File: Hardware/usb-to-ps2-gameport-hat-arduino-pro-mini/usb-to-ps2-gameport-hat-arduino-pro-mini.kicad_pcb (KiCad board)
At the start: 2 copper layers, 50 x 40 mm, 27 parts, among them P1 Digital, P2 Analog

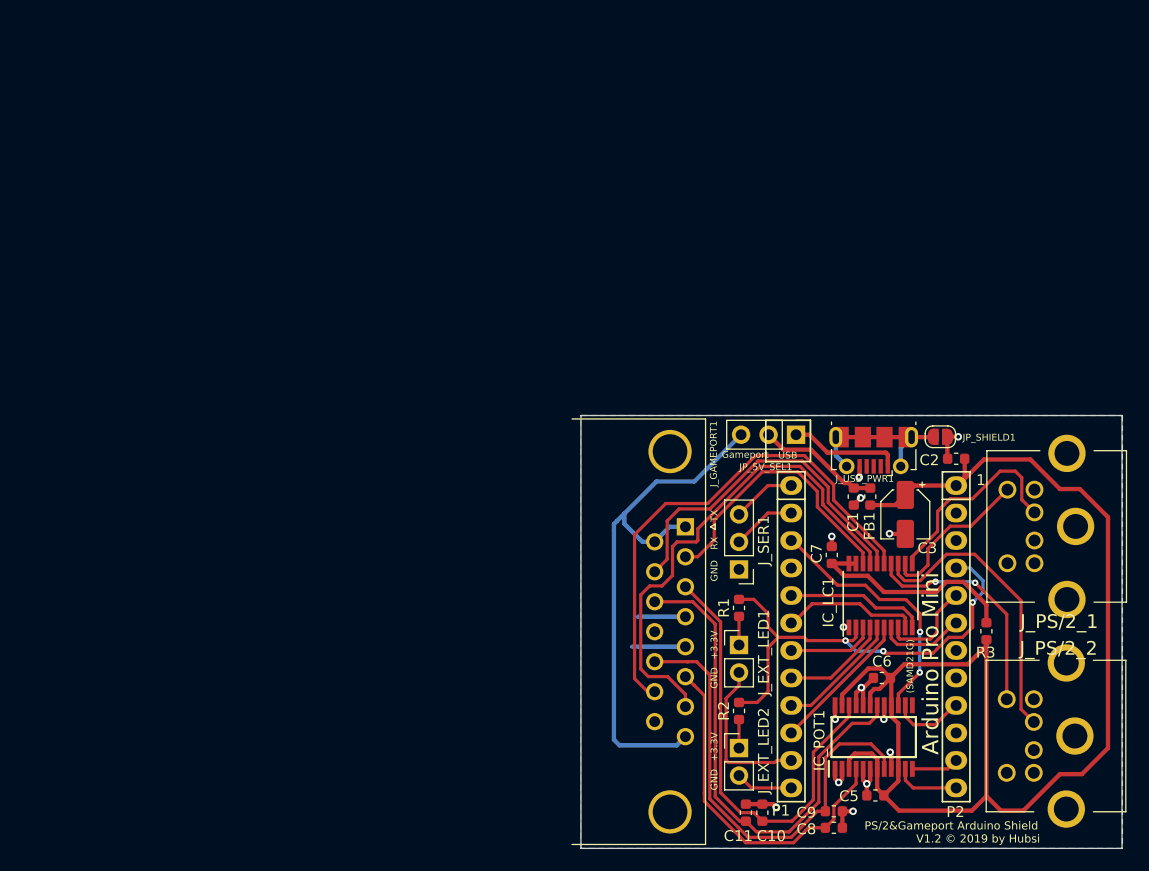
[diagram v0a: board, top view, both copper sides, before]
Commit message: update to KiCad 6
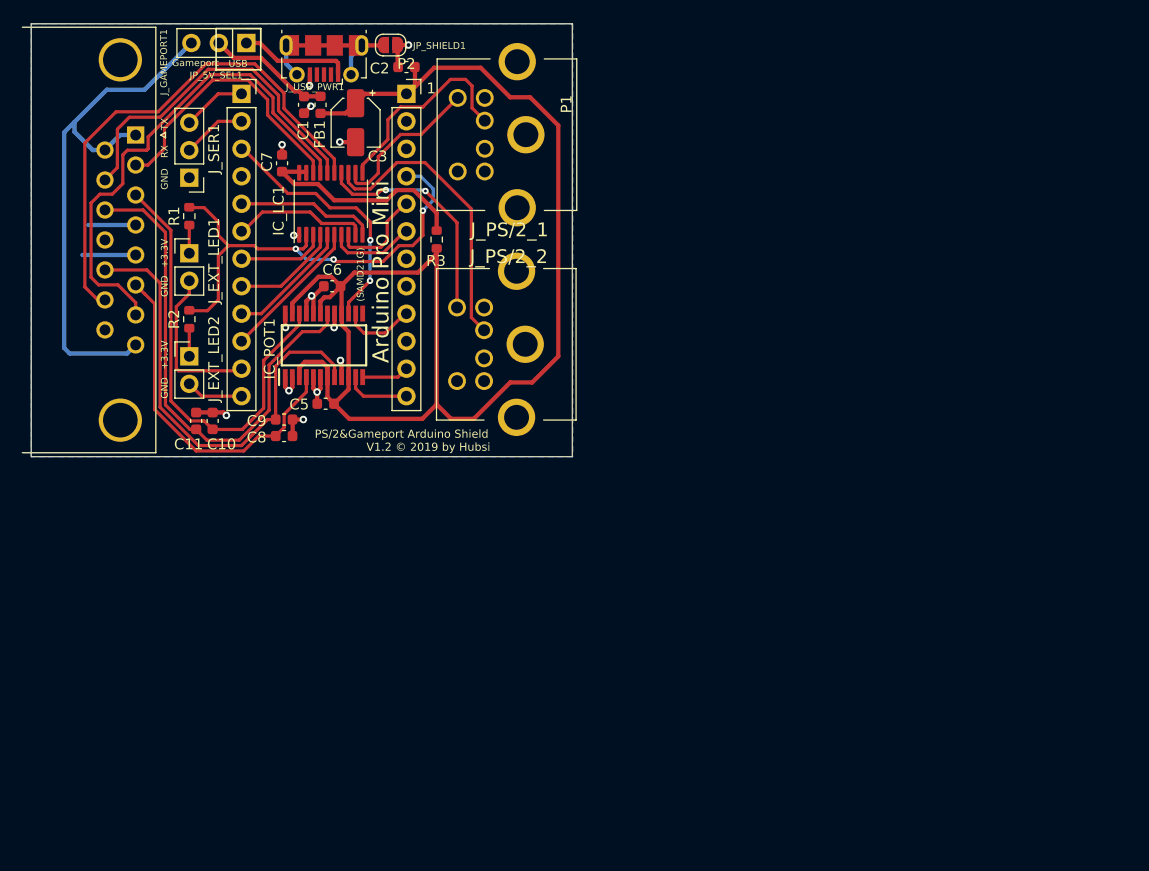
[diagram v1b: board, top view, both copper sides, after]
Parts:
- P1, P2: footprint Socket_Arduino_Pro_Mini:Socket_Strip_Arduino_1x12 -> Connector_PinSocket_2.54mm:PinSocket_1x12_P2.54mm_Vertical
- moved C6 62.4 mm to (114.2, 62.4)
- moved C10 62.4 mm to (103.1, 74.8)
- moved C11 62.4 mm to (101.6, 74.8)
- moved C3 62.4 mm to (116.3, 47.2)
- moved C7 62.4 mm to (109.5, 51.0)
- moved IC_POT1 62.4 mm to (113.4, 67.8)
- moved JP_5V_SEL1 62.4 mm to (106.2, 39.9)
- moved J_GAMEPORT1 62.4 mm to (96.0, 48.4)
- moved J_USB_PWR1 62.4 mm to (113.4, 41.3)
- moved P1 62.4 mm to (105.8, 44.6), turned to 0 degrees
- moved C8 62.4 mm to (109.7, 76.2)
- moved IC_LC1 62.4 mm to (114.0, 54.7)
- moved C2 62.4 mm to (121.0, 42.1)
- moved C5 62.4 mm to (113.6, 73.2)
- moved J_EXT_LED1 62.4 mm to (101.0, 59.3)
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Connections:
- IC_POT1 pad 13: (no net) -> unconnected-(IC_POT1-Pad13)
- J_GAMEPORT1 pad 12: (no net) -> unconnected-(J_GAMEPORT1-Pad12)
- J_GAMEPORT1 pad 15: (no net) -> unconnected-(J_GAMEPORT1-Pad15)
- J_PS/2_1 pad 2: (no net) -> unconnected-(J_PS/2_1-Pad2)
- J_PS/2_1 pad 4: (no net) -> unconnected-(J_PS/2_1-Pad4)
- J_PS/2_1 pad 6: (no net) -> unconnected-(J_PS/2_1-Pad6)
- J_PS/2_2 pad 2: (no net) -> unconnected-(J_PS/2_2-Pad2)
- J_PS/2_2 pad 4: (no net) -> unconnected-(J_PS/2_2-Pad4)
- J_PS/2_2 pad 6: (no net) -> unconnected-(J_PS/2_2-Pad6)
- J_USB_PWR1 pad 2: (no net) -> unconnected-(J_USB_PWR1-Pad2)
- J_USB_PWR1 pad 3: (no net) -> unconnected-(J_USB_PWR1-Pad3)
- J_USB_PWR1 pad 4: (no net) -> unconnected-(J_USB_PWR1-Pad4)
- P2 pad 10: (no net) -> /D12(MISO)
- P2 pad 3: (no net) -> unconnected-(P2-Pad3)
- P2 pad 7: (no net) -> unconnected-(P2-Pad7)
- P2 pad 8: (no net) -> unconnected-(P2-Pad8)
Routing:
- net +5V: track 130.0 -> 129.1 mm
- net /D5(JoyButton2): track 10.5 -> 9.83 mm
- net VCC: track 44.1 -> 43.6 mm
- net Net-(IC_LC1-Pad11): track 19.6 -> 19.1 mm
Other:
- net class Default removed
- net class Pwr removed

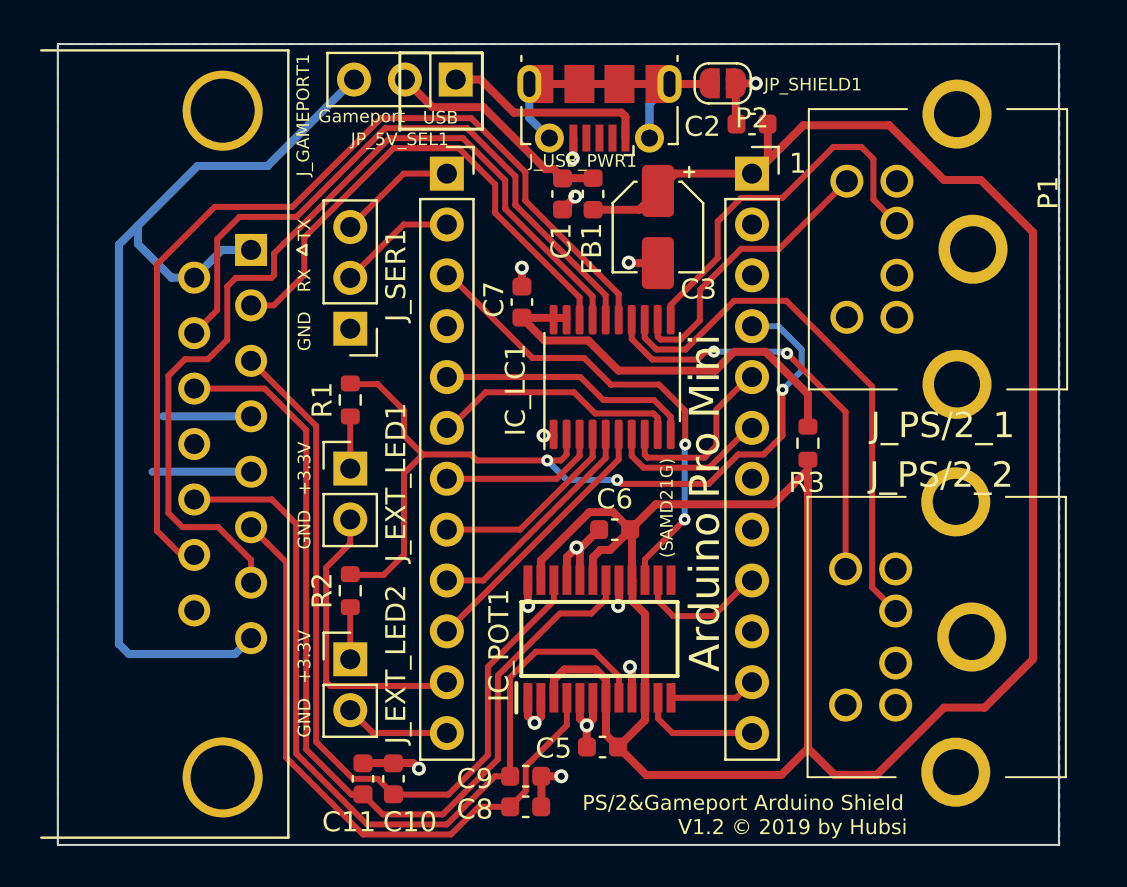
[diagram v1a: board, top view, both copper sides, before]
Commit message: Merge PR#1 from @Ulfenknulfen
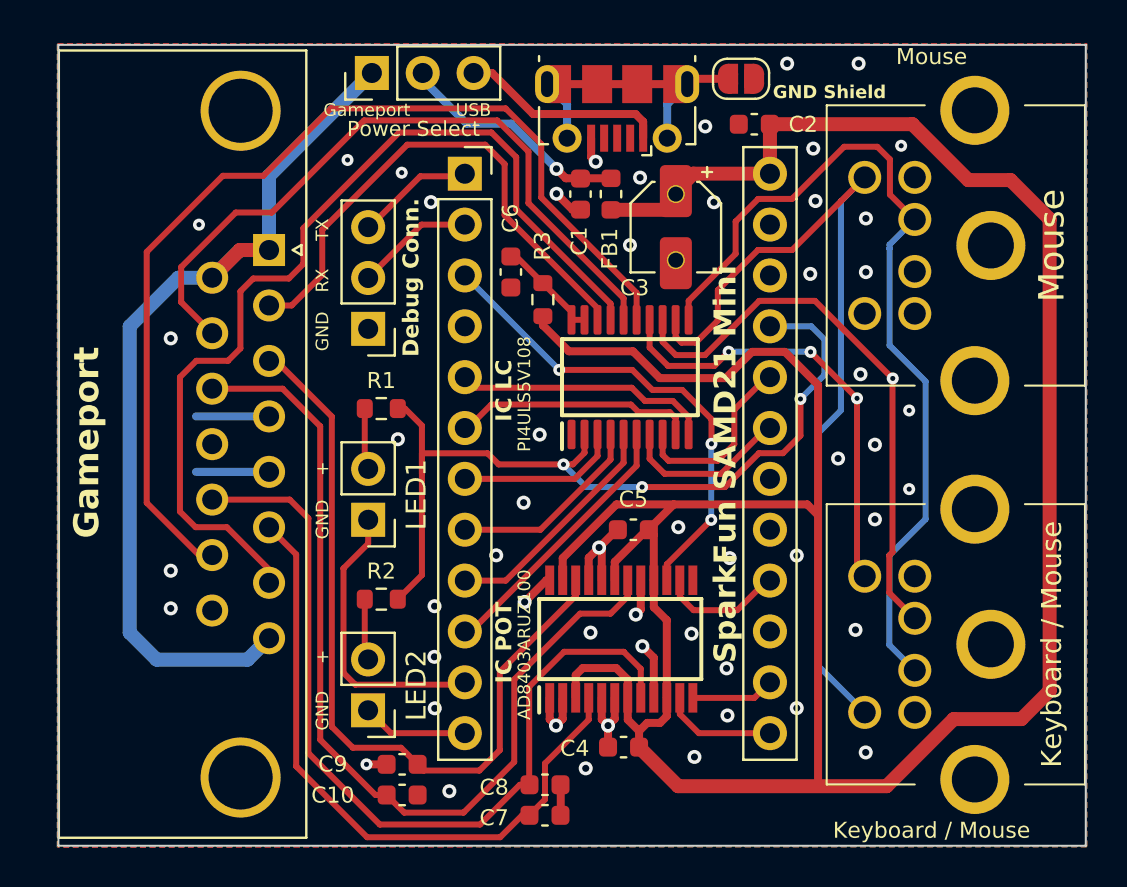
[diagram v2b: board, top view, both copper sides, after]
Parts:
- removed J_EXT_LED1, J_EXT_LED2: 2-pin header, Connector_PinHeader_2.54mm:PinHeader_1x02_P2.54mm_Vertical
- added ?: , , F.Cu at (117.2, 45.6)
- added ?: , , F.Cu at (117.2, 48.9)
- added LED1: 2-pin header, Connector_PinHeader_2.54mm:PinHeader_1x02_P2.54mm_Vertical, F.Cu at (101.9, 61.9)
- added LED2: 2-pin header, Connector_PinHeader_2.54mm:PinHeader_1x02_P2.54mm_Vertical, F.Cu at (101.9, 71.4)
- 5V Select1: renamed from JP_5V_SEL1
- Debug Conn1: renamed from J_SER1
- J_PS/2_1: value KMDGX-6S-BS -> Mouse
- J_PS/2_2: value KMDGX-6S-BS -> Keyboard / Mouse
- Shield GND1: renamed from JP_SHIELD1
- USB Power1: renamed from J_USB_PWR1
- moved R3 15.1 mm to (110.6, 50.9)
- moved 5V Select1 4.20 mm to (102.0, 39.5), turned to 90 degrees
- moved C10 2.12 mm to (103.6, 75.6), turned to 0 degrees
- moved R1 1.61 mm to (102.5, 56.3), turned to 180 degrees
- moved R2 1.61 mm to (102.5, 65.8), turned to 180 degrees
- moved C6 1.60 mm to (109.0, 49.5), turned to -90 degrees
- moved IC_POT1 1.09 mm to (114.5, 67.8)
- moved C4 1.05 mm to (114.6, 73.2)
- moved C7 1.05 mm to (110.7, 76.6)
- moved C8 1.05 mm to (110.7, 75.1)
- moved J_PS/2_2 1.02 mm to (129.2, 66.8)
- moved Shield GND1 0.94 mm to (120.5, 39.8)
- moved C5 0.93 mm to (115.1, 62.4)
- moved J_PS/2_1 0.91 mm to (129.2, 46.9)
- moved Gameport1 0.90 mm to (96.9, 48.4)
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- renumbered C11 to C10, C5 to C4, C6 to C5, C7 to C6, C8 to C7, C9 to C8, C10 to C9, J_GAMEPORT1 to Gameport1
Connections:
- 5V Select1 pad 1: /+5V(USB) -> /+5V(Gameport)
- 5V Select1 pad 2: Net-(C1-Pad1) -> unconnected-(5V Select1-C-Pad2)
- 5V Select1 pad 3: /+5V(Gameport) -> /+5V(USB)
- IC_LC1 pad 11: Net-(IC_LC1-Pad11) -> Net-(IC_LC1-B8)
- IC_LC1 pad 12: Net-(IC_LC1-Pad12) -> Net-(IC_LC1-B7)
- J_PS/2_1 pad 1: Net-(IC_LC1-Pad11) -> Net-(IC_LC1-B8)
- J_PS/2_1 pad 5: Net-(IC_LC1-Pad12) -> Net-(IC_LC1-B7)
- J_PS/2_2 pad 2: unconnected-(J_PS/2_2-Pad2) -> Net-(IC_LC1-B8)
- J_PS/2_2 pad 6: unconnected-(J_PS/2_2-Pad6) -> Net-(IC_LC1-B7)
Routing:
- net Net-(IC_LC1-B8): track 0.00 -> 43.9 mm
- net Net-(IC_LC1-B7): track 0.00 -> 43.5 mm
- net +5V: track 129.1 -> 149.0 mm
- net Net-(IC_LC1-Pad11): track 19.1 -> 0.00 mm
- net Net-(IC_LC1-EN): track 20.5 -> 5.23 mm
- net Net-(IC_LC1-Pad12): track 14.6 -> 0.00 mm
- net GND: track 38.7 -> 31.0 mm, vias 14 -> 54
- net /+5V(Gameport): track 50.1 -> 46.2 mm
- net Net-(Gameport1-P14): track 47.4 -> 51.0 mm
- net Net-(Gameport1-P10): track 32.3 -> 35.2 mm
- net Net-(IC_LC1-B2): track 46.6 -> 48.1 mm
- net /W1(Joy1X): track 41.0 -> 39.6 mm
- net Net-(IC_LC1-B6): track 27.1 -> 28.3 mm, vias 0 -> 1
- net Net-(IC_LC1-B5): track 21.4 -> 22.5 mm, vias 2 -> 3
- net /W2(Joy1Y): track 32.2 -> 33.2 mm
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- added copper zone on F.Cu, net GND
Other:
- board size 50 x 40 mm -> 51.3 x 40 mm
- board text added: "+"
- board text added: "Debug Conn."
- board text added: "GND Shield"
- board text added: "IC LC"
- board text added: "IC POT"
- board text added: "Keyboard / Mouse"
- board text added: "Mouse"
- board text added: "Power"
- board text added: "Power Select"
- board text added: "SparkFun SAMD21 Mini"
- board text added: "V1.3 © 2024 by Hubsi"
- board text removed: "(SAMD21G)"
- board text removed: "+3.3V"
- board text removed: "1"
- board text removed: "Arduino Pro Mini"
- board text removed: "V1.2 © 2019 by Hubsi"

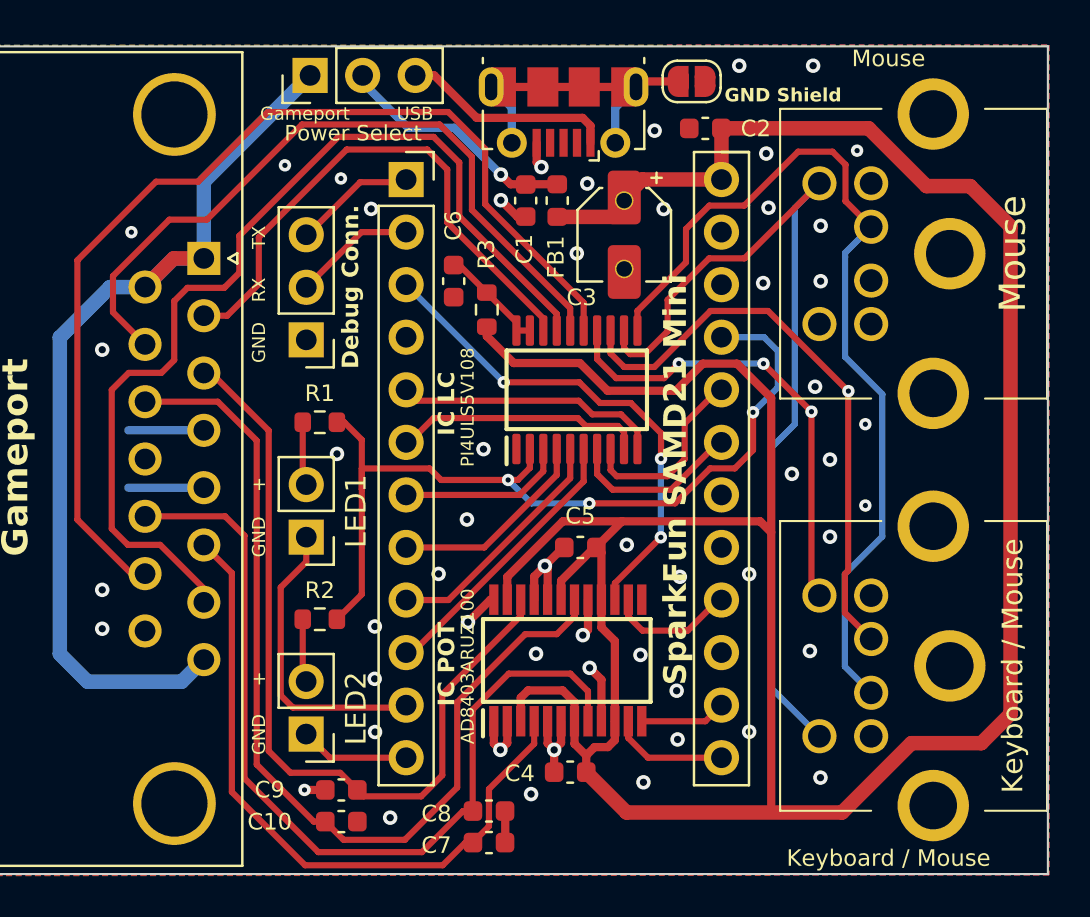
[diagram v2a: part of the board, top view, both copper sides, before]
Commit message: @Ulfenknulfen: connect base of digi-pot with wiper
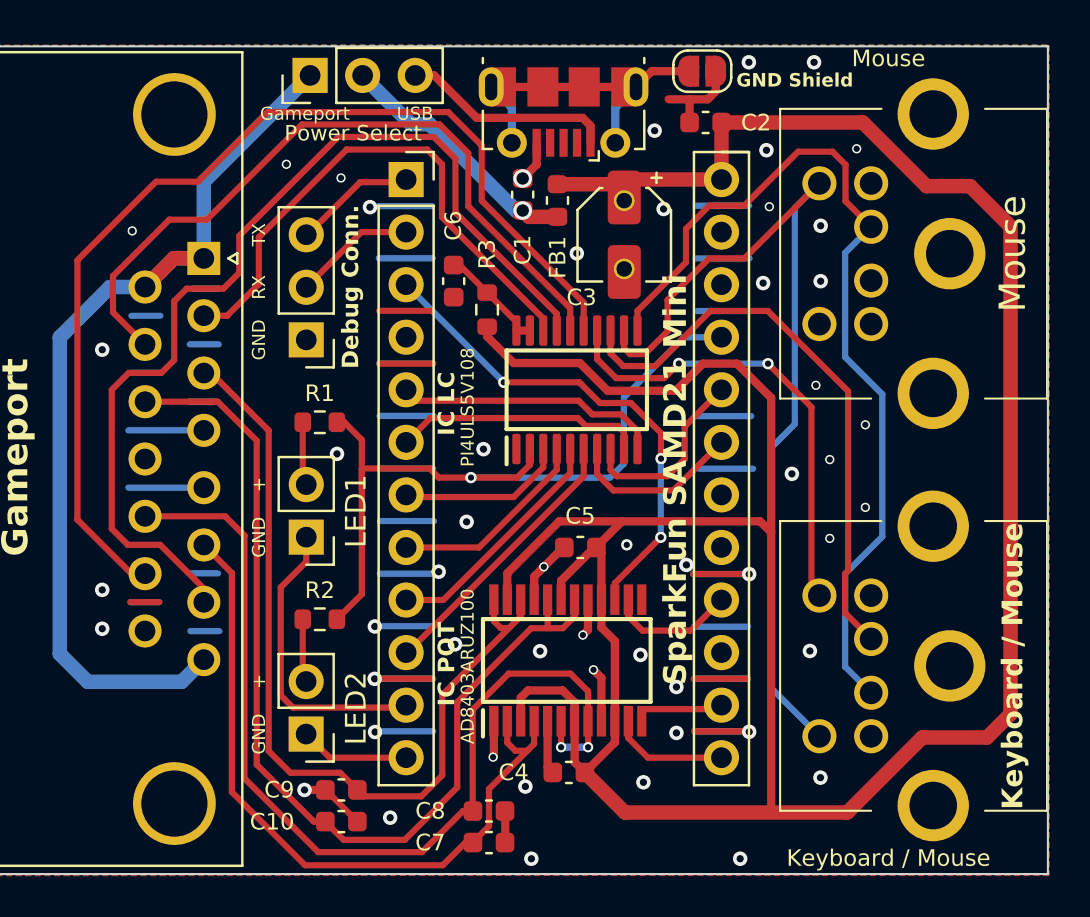
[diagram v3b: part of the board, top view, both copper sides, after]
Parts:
- moved Shield GND1 0.71 mm to (121.0, 39.3)
- moved C1 0.33 mm to (112.3, 45.3), turned to 90 degrees
- moved C2 0.29 mm to (121.2, 41.8)
- moved C4 0.07 mm to (114.5, 73.2)
- turned FB1 to -90 degrees
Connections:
- 5V Select1 pad 2: unconnected-(5V Select1-C-Pad2) -> Net-(C1-Pad1)
- IC_POT1 pad 2: GND -> /W2(Joy1Y)
- IC_POT1 pad 20: GND -> /W3(Joy2X)
- IC_POT1 pad 24: GND -> /W1(Joy1X)
- IC_POT1 pad 6: GND -> /W4(Joy2Y)
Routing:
- net GND: track 31.0 -> 110.8 mm, vias 54 -> 53
- net VCC: track 42.8 -> 37.8 mm, vias 3 -> 1
- net /W4(Joy2Y): track 43.3 -> 47.1 mm, vias 0 -> 2
- net /W2(Joy1Y): track 33.2 -> 35.3 mm
- net /W1(Joy1X): track 39.6 -> 41.4 mm
- net /W3(Joy2X): track 46.4 -> 47.8 mm
- net Net-(Shield GND1-A): track 15.1 -> 16.1 mm
- net Net-(C1-Pad1): track 11.5 -> 12.3 mm
- net +5V: track 149.0 -> 149.6 mm
- net Net-(IC_LC1-B5): track 22.5 -> 22.6 mm, vias 3 -> 2
- net Net-(IC_LC1-B6): track 28.3 -> 28.2 mm, vias 1 -> 0
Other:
- board text added: "PS/2&Gameport Arduino Shield V1.4 © 2024 by Hubsi Thanks to Paddy"
- board text removed: "PS/2&Gameport Arduino Shield"
- board text removed: "V1.3 © 2024 by Hubsi"
